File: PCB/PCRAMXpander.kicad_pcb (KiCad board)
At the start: 2 copper layers, 134.6 x 97.8 mm, 22 parts, among them J1 Bus_ISA_16bit, U1 ATF16V8B-15PU, U2 SN74LVCR16245ADGGR, U3 SN74LVC16244ADGGR, U4 SN74LVC16244ADGGR, U5 AS6C3216A-55TIN, U6 AS6C3216A-55TIN

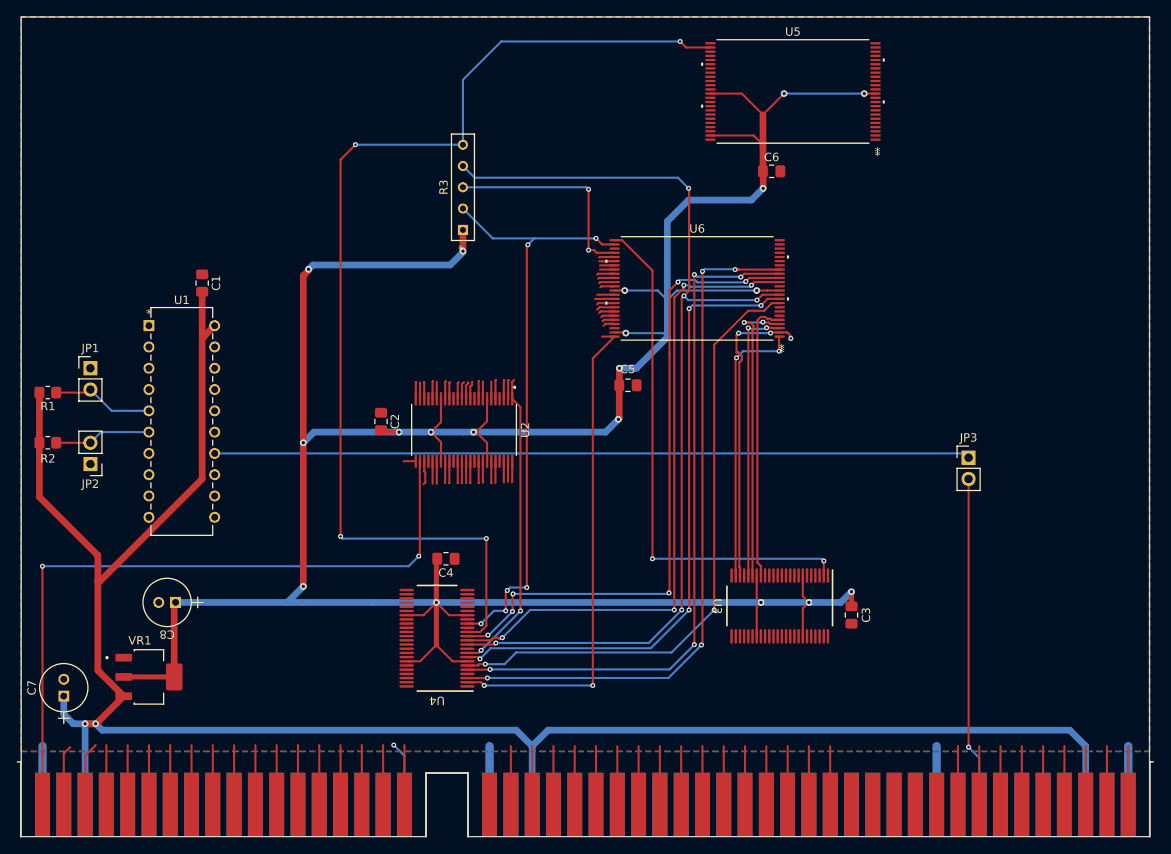
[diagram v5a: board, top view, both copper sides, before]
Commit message: Memory chips routed
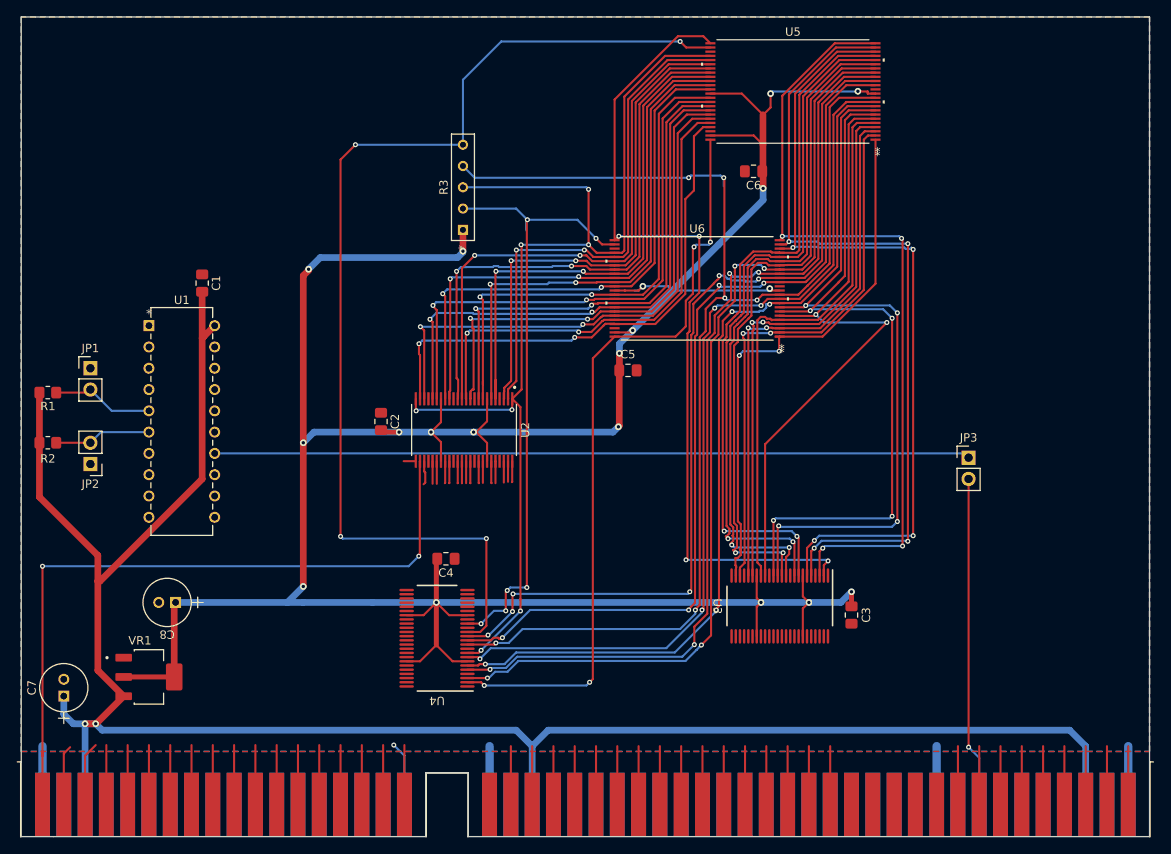
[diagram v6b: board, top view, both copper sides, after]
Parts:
- moved C6 2.16 mm to (150.9, 73.0), turned to 180 degrees
- moved C5 1.78 mm to (135.9, 96.8)
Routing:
- net A3: track 0.00 -> 97.2 mm, vias 0 -> 4
- net A2: track 0.00 -> 96.2 mm, vias 0 -> 4
- net A1: track 0.00 -> 95.2 mm, vias 0 -> 4
- net A8: track 0.00 -> 88.6 mm, vias 0 -> 4
- net A9: track 0.00 -> 86.9 mm, vias 0 -> 4
- net A4: track 0.00 -> 83.9 mm, vias 0 -> 2
- net A5: track 0.00 -> 82.8 mm, vias 0 -> 2
- net A6: track 0.00 -> 81.4 mm, vias 0 -> 2
- net A7: track 0.00 -> 79.7 mm, vias 0 -> 2
- net A10: track 0.00 -> 77.3 mm, vias 0 -> 2
- net OE: track 64.0 -> 132.4 mm, vias 4 -> 7
- net D9: track 3.79 -> 66.5 mm, vias 0 -> 2
- net D8: track 3.94 -> 66.6 mm, vias 0 -> 2
- net D10: track 4.04 -> 66.0 mm, vias 0 -> 2
- net D11: track 3.92 -> 65.6 mm, vias 0 -> 2
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
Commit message: Low data lines routed
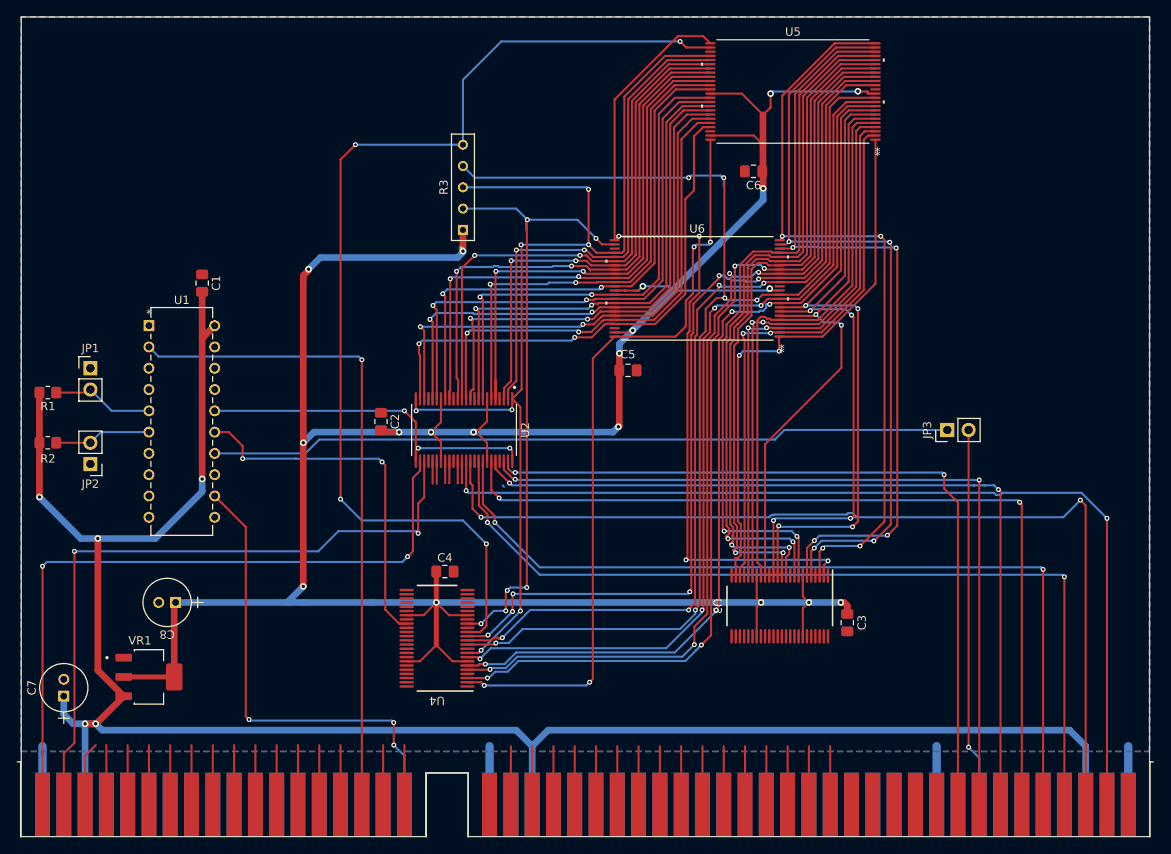
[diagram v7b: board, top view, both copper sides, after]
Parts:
- moved JP3 4.17 mm to (174.0, 103.9), turned to 90 degrees
- moved C4 1.53 mm to (114.0, 120.8)
- moved C3 1.04 mm to (162.1, 126.9)
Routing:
- net Net-(J1-DB6): track 9.62 -> 116.7 mm, vias 0 -> 2
- net Net-(J1-DB7): track 9.61 -> 115.7 mm, vias 0 -> 2
- net Net-(J1-DB5): track 9.63 -> 106.5 mm, vias 0 -> 2
- net Net-(J1-DB4): track 9.58 -> 103.7 mm, vias 0 -> 2
- net Net-(J1-DB3): track 9.64 -> 103.5 mm, vias 0 -> 2
- net Net-(J1-DB2): track 9.62 -> 99.7 mm, vias 0 -> 2
- net Net-(J1-DB1): track 9.54 -> 97.0 mm, vias 0 -> 2
- net Net-(J1-DB0): track 9.45 -> 93.3 mm, vias 0 -> 2
- net LA22: track 7.11 -> 79.1 mm, vias 0 -> 1
- net Net-(J1-D14): track 10.1 -> 81.8 mm, vias 0 -> 2
- net MEMCS16: track 7.64 -> 56.1 mm, vias 1 -> 3
- net CS_HI: track 0.00 -> 43.4 mm, vias 0 -> 2
- net TRANS_EN: track 3.97 -> 43.5 mm, vias 0 -> 3
- net A8: track 88.6 -> 79.3 mm
- net A9: track 86.9 -> 77.9 mm
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
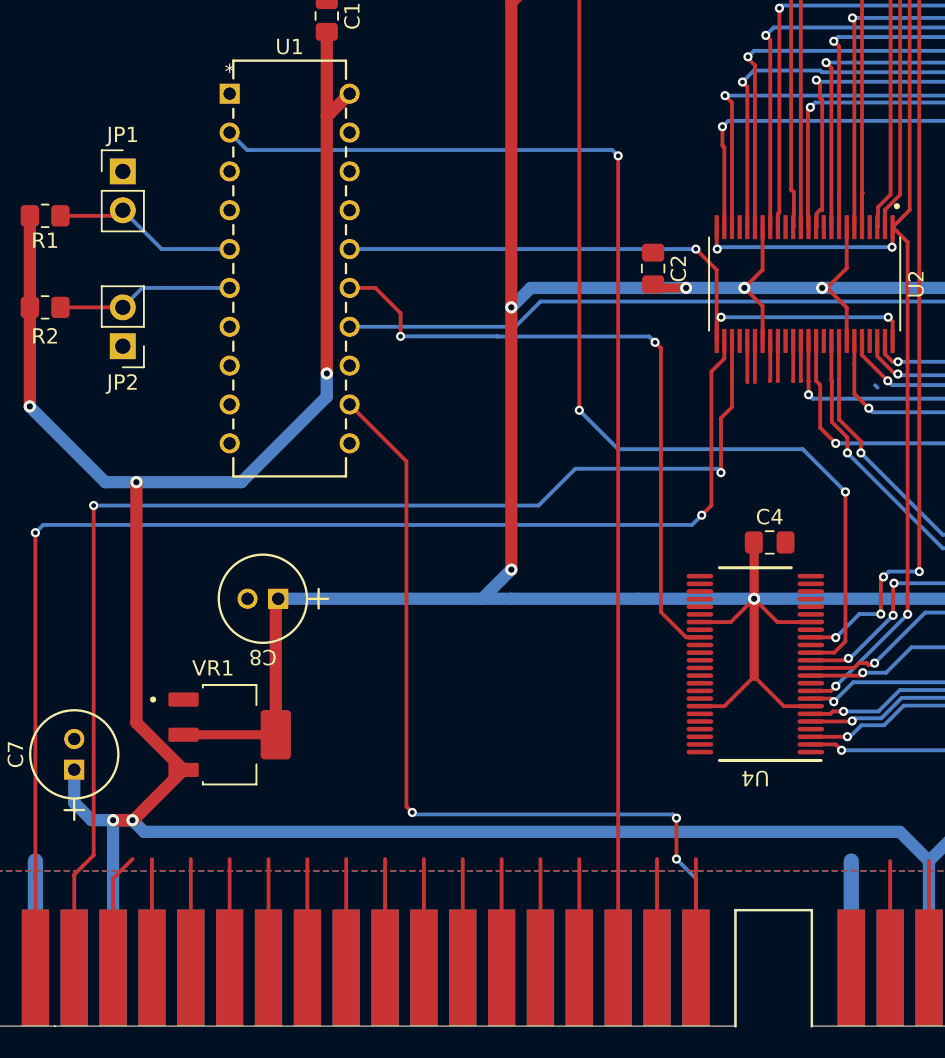
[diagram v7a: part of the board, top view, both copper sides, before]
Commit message: GAL and U4 routes
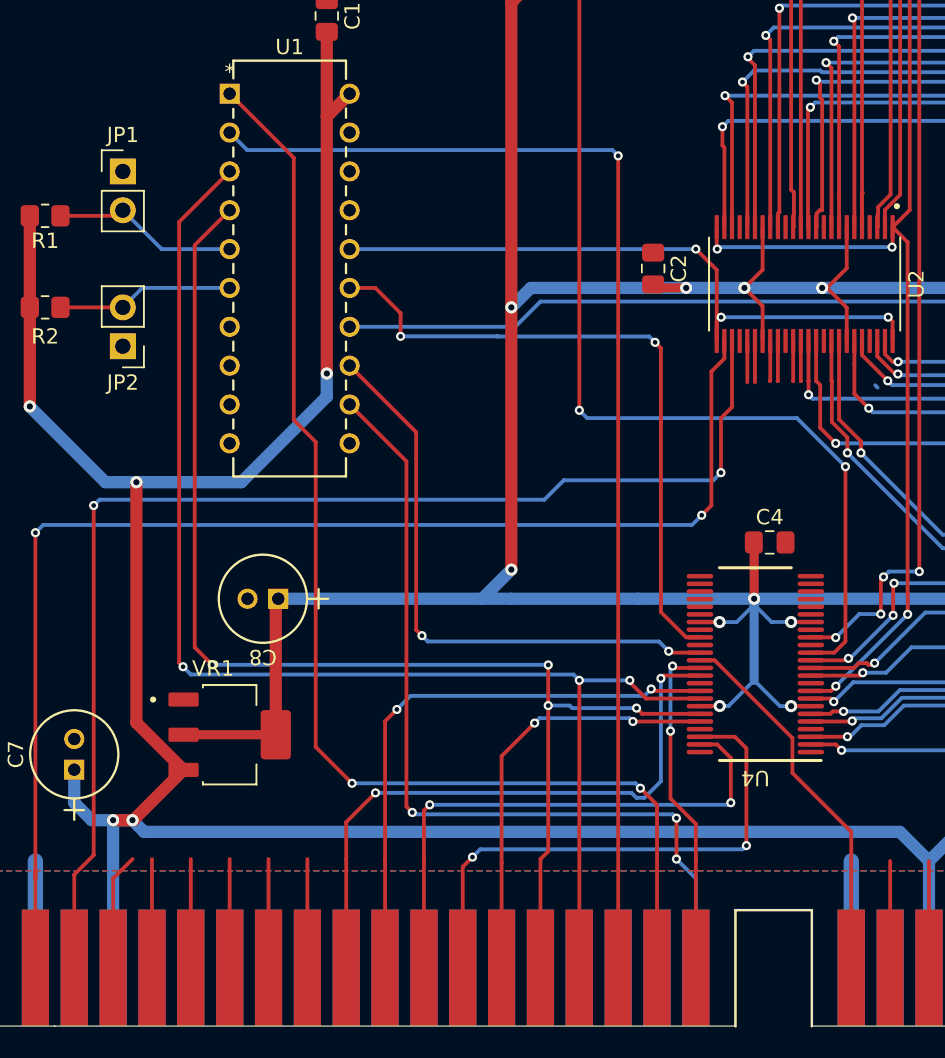
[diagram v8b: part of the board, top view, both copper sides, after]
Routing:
- net LA21: track 7.11 -> 87.4 mm, vias 0 -> 3
- net LA20: track 7.11 -> 83.3 mm, vias 0 -> 4
- net LA23: track 7.11 -> 79.6 mm, vias 0 -> 2
- net CS_LO: track 0.00 -> 38.2 mm, vias 0 -> 2
- net MEMW: track 7.11 -> 40.8 mm, vias 0 -> 2
- net MEMR: track 7.11 -> 37.8 mm, vias 0 -> 2
- net LA17: track 7.11 -> 36.1 mm, vias 0 -> 2
- net LA18: track 7.11 -> 35.4 mm, vias 0 -> 2
- net BA00: track 0.00 -> 24.8 mm
- net LA19: track 7.11 -> 27.9 mm, vias 0 -> 2
- net SBHE: track 7.11 -> 22.4 mm, vias 0 -> 2
- net C1E: track 127.3 -> 128.2 mm
- net +3.3V: track 356.9 -> 356.6 mm, vias 19 -> 23
